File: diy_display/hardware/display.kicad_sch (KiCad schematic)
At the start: 16 parts, among them J1 Connector_1, U2 ESP32-C3-MINI-1

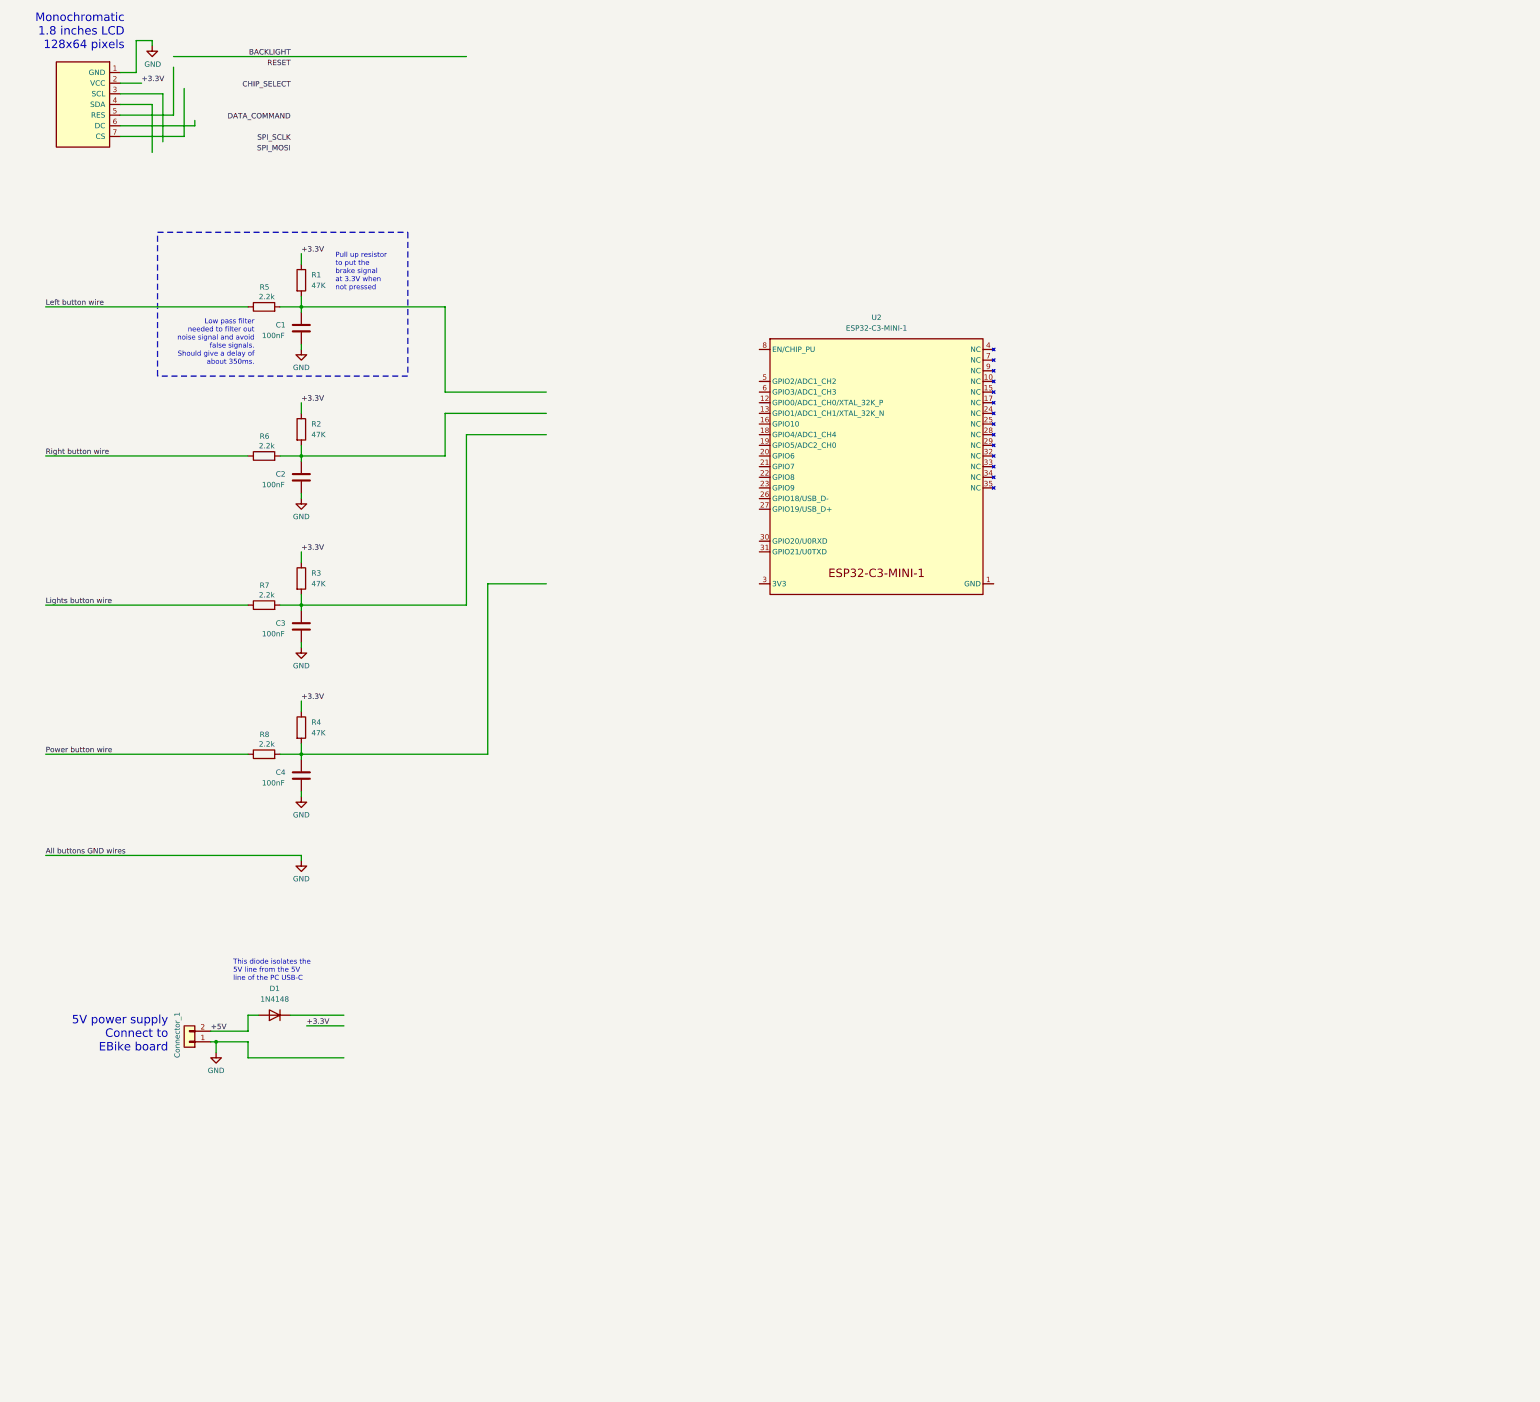
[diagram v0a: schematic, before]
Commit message: Updated display schematic based on latest version
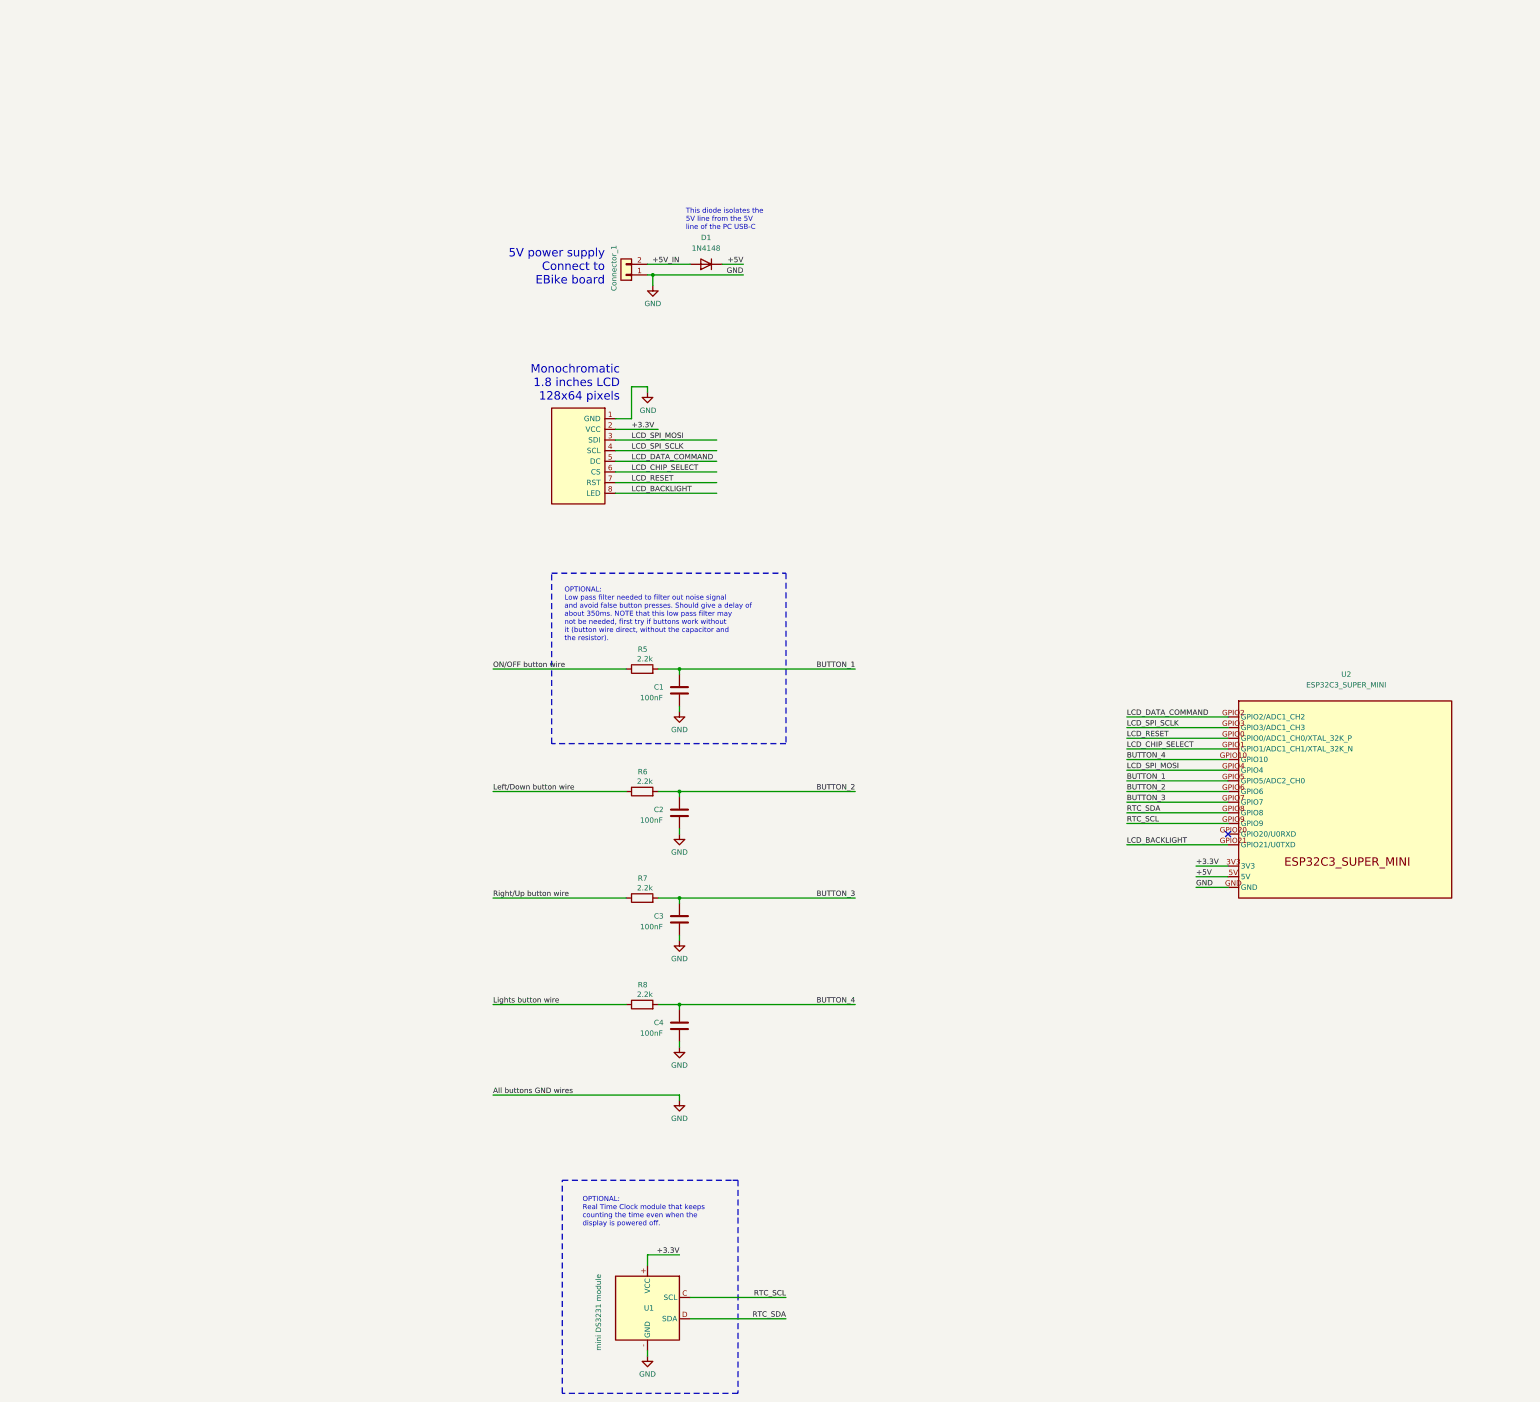
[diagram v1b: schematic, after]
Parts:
- removed R1, R2, R3, R4: 47K, symbol Device:R
- added U1: mini DS3231 module, symbol mini_ds3231_module:mini_DS3231_module
- NA1: value OLED_1.3_inches_128x64 -> Monochromatic_1.8 _inches_LCD_128x64_pixels
- U2: value ESP32-C3-MINI-1 -> ESP32C3_SUPER_MINI; footprint Espressif:ESP32-C3-MINI-1 -> (none)
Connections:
- net Power button wire is gone; now on net Lights button wire: R8.1
- net +3.3V: now also U2.3V3, U1.+ (VCC)
- net +5V: now also D1.1 (K), U2.5V; no longer D1.2 (A), J1.2 (Pin_2)
- net GND: now also U2.GND, U1.- (GND)
- net Lights button wire: no longer R7.1
- net BUTTON_2: now reaches C2.1, R6.2
- net BUTTON_2: now also U2.GPIO6
- net BUTTON_1: now reaches C1.1, R5.2
- net BUTTON_1: now also U2.GPIO5 (GPIO5/ADC2_CH0)
- net BUTTON_4: now reaches C4.1, R8.2
- net BUTTON_4: now also U2.GPIO10
- net BUTTON_3: now reaches C3.1, R7.2
- net BUTTON_3: now also U2.GPIO7
- net LCD_SPI_MOSI: now reaches NA1.3 (SDI)
- net LCD_SPI_MOSI: now also U2.GPIO4
- net LCD_SPI_SCLK: now reaches NA1.4 (SCL)
- net LCD_SPI_SCLK: now also U2.GPIO3 (GPIO3/ADC1_CH3)
- net LCD_DATA_COMMAND: now reaches NA1.5 (DC)
- net LCD_DATA_COMMAND: now also U2.GPIO2 (GPIO2/ADC1_CH2)
- net LCD_CHIP_SELECT: now reaches NA1.6 (CS)
- net LCD_CHIP_SELECT: now also U2.GPIO1 (GPIO1/ADC1_CH1/XTAL_32K_N)
- net LCD_RESET: now reaches NA1.7 (RST)
- net LCD_RESET: now also U2.GPIO0 (GPIO0/ADC1_CH0/XTAL_32K_P)
- net Left button wire renamed ON/OFF button wire
- net Right button wire renamed Left/Down button wire
- new net +5V_IN: D1.2 (A), J1.2 (Pin_2)
- new net LCD_BACKLIGHT: NA1.8 (LED), U2.GPIO21 (GPIO21/U0TXD)
- new net RTC_SCL: U1.C (SCL), U2.GPIO9
- new net RTC_SDA: U1.D (SDA), U2.GPIO8
- new net Right/Up button wire: R7.1
- no-connect marks 0 -> 1
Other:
- note added: "OPTIONAL: Low pass filter needed to filter out noise signal and avoid false button presses. Should give a delay of about 350ms. NOTE that this low pass filter may not be needed, first try if buttons work without it (button wire direct, without the capacitor and the resistor)."
- note added: "OPTIONAL: Real Time Clock module that keeps counting the time even when the display is powered off."
- note removed: "Low pass filter needed to filter out noise signal and avoid false signals. Should give a delay of about 350ms."
- note removed: "Pull up resistor to put the brake signal at 3.3V when not pressed"
- moved on the sheet: C1, C2, C3, C4, D1, R5, R6, R7, R8

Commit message: Cosmetic changes to display schematic
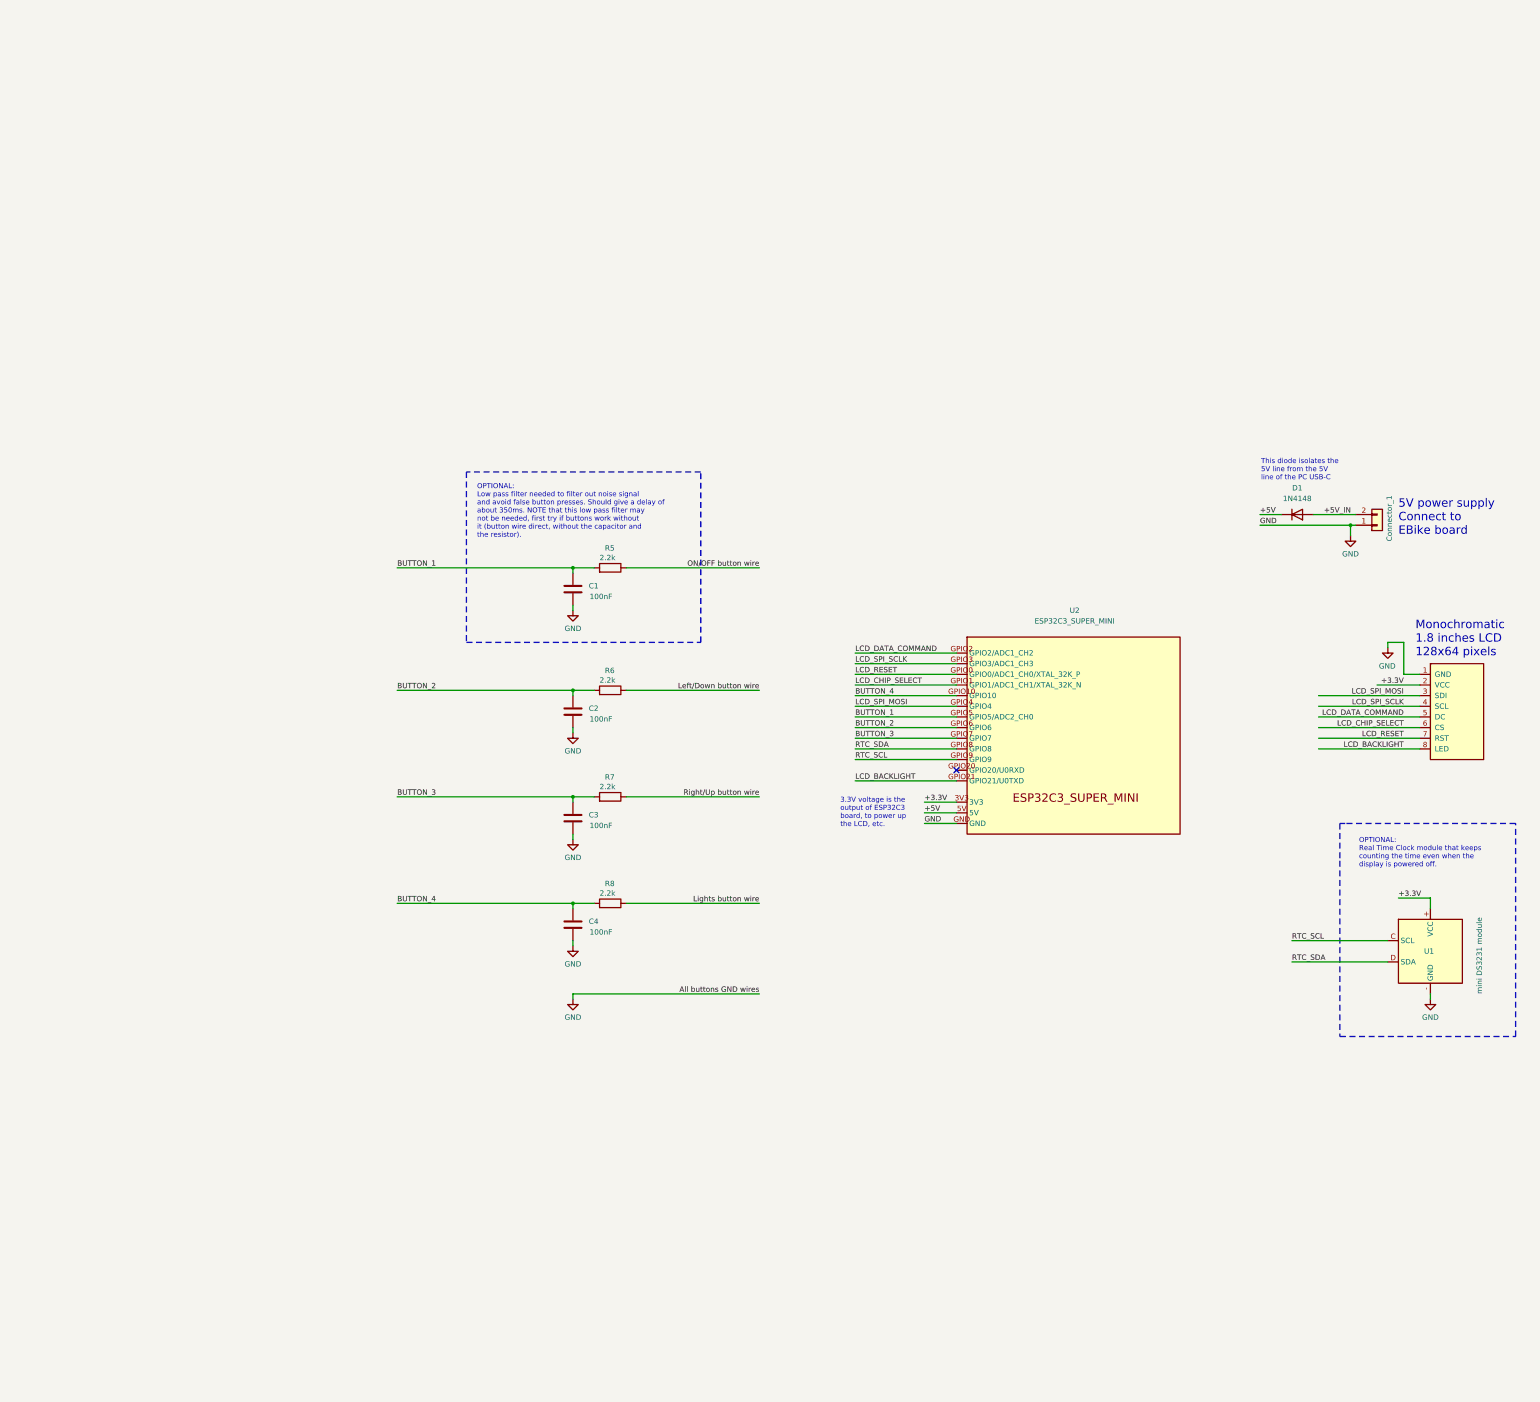
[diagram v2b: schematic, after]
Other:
- note added: "3.3V voltage is the output of ESP32C3 board, to power up the LCD, etc."
- moved on the sheet: C1, C2, C3, C4, D1, R5, R6, R7, R8, U1, U2
